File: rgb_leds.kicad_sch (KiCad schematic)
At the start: 14 parts

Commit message: Reannotate the board
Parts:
- renumbered C1401 to C55, C1402 to C56, C1403 to C57, C1404 to C58, C1405 to C59, C1406 to C60, D1401 to D15, D1402 to D16, LED1401 to LED1, LED1402 to LED2, LED1403 to LED3, LED1404 to LED4, LED1405 to LED5, TP1401 to TP26
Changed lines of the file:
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@@
 		(dnp no)
 		(fields_autoplaced yes)
-		(property "Reference" "C1403"
+		(property "Reference" "C57"
 			(at 125.73 119.3799 0)
 			(effects
@@
 			(project "HALPI2"
 				(path "/abc482bd-3f17-4d35-80db-1da3dcdb5c27/850df4bf-e40a-4082-adc2-76804638b949/7441bc5f-8874-43c2-af8a-50459ea25028"
-					(reference "C1403")
+					(reference "C57")
 					(unit 1)
 				)
@@
 		(on_board yes)
 		(dnp no)
-		(property "Reference" "#PWR01403"
+		(property "Reference" "#PWR077"
 			(at 97.79 130.81 0)
 			(effects
@@
 			(project "HALPI2"
 				(path "/abc482bd-3f17-4d35-80db-1da3dcdb5c27/850df4bf-e40a-4082-adc2-76804638b949/7441bc5f-8874-43c2-af8a-50459ea25028"
-					(reference "#PWR01403")
+					(reference "#PWR077")
 					(unit 1)
 				)
@@
 		(dnp no)
 		(fields_autoplaced yes)
-		(property "Reference" "C1405"
+		(property "Reference" "C59"
 			(at 156.21 119.3799 0)
 			(effects
@@
 			(project "HALPI2"
 				(path "/abc482bd-3f17-4d35-80db-1da3dcdb5c27/850df4bf-e40a-4082-adc2-76804638b949/7441bc5f-8874-43c2-af8a-50459ea25028"
-					(reference "C1405")
+					(reference "C59")
 					(unit 1)
 				)
@@
 		(dnp no)
 		(fields_autoplaced yes)
-		(property "Reference" "C1404"
+		(property "Reference" "C58"
 			(at 140.97 119.3799 0)
 			(effects
@@
 			(project "HALPI2"
 				(path "/abc482bd-3f17-4d35-80db-1da3dcdb5c27/850df4bf-e40a-4082-adc2-76804638b949/7441bc5f-8874-43c2-af8a-50459ea25028"
-					(reference "C1404")
+					(reference "C58")
 					(unit 1)
 				)
@@
 		(on_board yes)
 		(dnp no)
-		(property "Reference" "#PWR01407"
+		(property "Reference" "#PWR081"
 			(at 152.4 130.81 0)
 			(effects
@@
 			(project "HALPI2"
 				(path "/abc482bd-3f17-4d35-80db-1da3dcdb5c27/850df4bf-e40a-4082-adc2-76804638b949/7441bc5f-8874-43c2-af8a-50459ea25028"
-					(reference "#PWR01407")
+					(reference "#PWR081")
 					(unit 1)
 				)
@@
 		(dnp no)
 		(fields_autoplaced yes)
-		(property "Reference" "TP1401"
+		(property "Reference" "TP26"
 			(at 186.69 109.2199 90)
 			(effects
@@
 			(project "HALPI2"
 				(path "/abc482bd-3f17-4d35-80db-1da3dcdb5c27/850df4bf-e40a-4082-adc2-76804638b949/7441bc5f-8874-43c2-af8a-50459ea25028"
-					(reference "TP1401")
+					(reference "TP26")
 					(unit 1)
 				)
@@
 		(dnp no)
 		(fields_autoplaced yes)
-		(property "Reference" "#PWR01401"
+		(property "Reference" "#PWR075"
 			(at 81.28 105.41 0)
 			(effects
@@
 			(project ""
 				(path "/abc482bd-3f17-4d35-80db-1da3dcdb5c27/850df4bf-e40a-4082-adc2-76804638b949/7441bc5f-8874-43c2-af8a-50459ea25028"
-					(reference "#PWR01401")
+					(reference "#PWR075")
 					(unit 1)
 				)
@@
 		(on_board yes)
 		(dnp no)
-		(property "Reference" "#PWR01404"
+		(property "Reference" "#PWR078"
 			(at 106.68 130.81 0)
 			(effects
@@
 			(project "HALPI2"
 				(path "/abc482bd-3f17-4d35-80db-1da3dcdb5c27/850df4bf-e40a-4082-adc2-76804638b949/7441bc5f-8874-43c2-af8a-50459ea25028"
-					(reference "#PWR01404")
+					(reference "#PWR078")
 					(unit 1)
 				)
@@
 		(dnp no)
 		(fields_autoplaced yes)
-		(property "Reference" "D1402"
+		(property "Reference" "D16"
 			(at 90.17 104.4574 90)
 			(effects
@@
 			(project ""
 				(path "/abc482bd-3f17-4d35-80db-1da3dcdb5c27/850df4bf-e40a-4082-adc2-76804638b949/7441bc5f-8874-43c2-af8a-50459ea25028"
-					(reference "D1402")
+					(reference "D16")
 					(unit 1)
 				)
@@
 		(dnp no)
 		(fields_autoplaced yes)
-		(property "Reference" "#PWR01402"
+		(property "Reference" "#PWR076"
 			(at 87.63 105.41 0)
 			(effects
@@
 			(project "HALPI2"
 				(path "/abc482bd-3f17-4d35-80db-1da3dcdb5c27/850df4bf-e40a-4082-adc2-76804638b949/7441bc5f-8874-43c2-af8a-50459ea25028"
-					(reference "#PWR01402")
+					(reference "#PWR076")
 					(unit 1)
 				)
@@
 		(on_board yes)
 		(dnp no)
-		(property "Reference" "#PWR01409"
+		(property "Reference" "#PWR083"
 			(at 180.34 123.19 0)
 			(effects
@@
 			(project "HALPI2"
 				(path "/abc482bd-3f17-4d35-80db-1da3dcdb5c27/850df4bf-e40a-4082-adc2-76804638b949/7441bc5f-8874-43c2-af8a-50459ea25028"
-					(reference "#PWR01409")
+					(reference "#PWR083")
 					(unit 1)
 				)
@@
 		(on_board yes)
 		(dnp no)
-		(property "Reference" "C1401"
+		(property "Reference" "C55"
 			(at 93.98 119.3799 0)
 			(effects
@@
 			(project "HALPI2"
 				(path "/abc482bd-3f17-4d35-80db-1da3dcdb5c27/850df4bf-e40a-4082-adc2-76804638b949/7441bc5f-8874-43c2-af8a-50459ea25028"
-					(reference "C1401")
+					(reference "C55")
 					(unit 1)
 				)
@@
 		(on_board yes)
 		(dnp no)
-		(property "Reference" "#PWR01408"
+		(property "Reference" "#PWR082"
 			(at 167.64 130.81 0)
 			(effects
@@
 			(project "HALPI2"
 				(path "/abc482bd-3f17-4d35-80db-1da3dcdb5c27/850df4bf-e40a-4082-adc2-76804638b949/7441bc5f-8874-43c2-af8a-50459ea25028"
-					(reference "#PWR01408")
+					(reference "#PWR082")
 					(unit 1)
 				)
@@
 		(on_board yes)
 		(dnp no)
-		(property "Reference" "LED1402"
+		(property "Reference" "LED2"
 			(at 116.332 78.74 90)
 			(effects
@@
 			(project "HALPI2"
 				(path "/abc482bd-3f17-4d35-80db-1da3dcdb5c27/850df4bf-e40a-4082-adc2-76804638b949/7441bc5f-8874-43c2-af8a-50459ea25028"
-					(reference "LED1402")
+					(reference "LED2")
 					(unit 1)
 				)
@@
 		(on_board yes)
 		(dnp no)
-		(property "Reference" "#PWR01406"
+		(property "Reference" "#PWR080"
 			(at 137.16 130.81 0)
 			(effects
@@
 			(project "HALPI2"
 				(path "/abc482bd-3f17-4d35-80db-1da3dcdb5c27/850df4bf-e40a-4082-adc2-76804638b949/7441bc5f-8874-43c2-af8a-50459ea25028"
-					(reference "#PWR01406")
+					(reference "#PWR080")
 					(unit 1)
 				)
@@
 		(on_board yes)
 		(dnp no)
-		(property "Reference" "D1401"
+		(property "Reference" "D15"
 			(at 78.74 104.4574 90)
 			(effects
@@
 			(project "HALPI2"
 				(path "/abc482bd-3f17-4d35-80db-1da3dcdb5c27/850df4bf-e40a-4082-adc2-76804638b949/7441bc5f-8874-43c2-af8a-50459ea25028"
-					(reference "D1401")
+					(reference "D15")
 					(unit 1)
 				)
@@
 		(on_board yes)
 		(dnp no)
-		(property "Reference" "LED1404"
+		(property "Reference" "LED4"
 			(at 148.082 78.74 90)
 			(effects
@@
 			(project "HALPI2"
 				(path "/abc482bd-3f17-4d35-80db-1da3dcdb5c27/850df4bf-e40a-4082-adc2-76804638b949/7441bc5f-8874-43c2-af8a-50459ea25028"
-					(reference "LED1404")
+					(reference "LED4")
 					(unit 1)
 				)
@@
 		(dnp no)
 		(fields_autoplaced yes)
-		(property "Reference" "#FLG01401"
+		(property "Reference" "#FLG011"
 			(at 79.375 114.3 0)
 			(effects
@@
 			(project ""
 				(path "/abc482bd-3f17-4d35-80db-1da3dcdb5c27/850df4bf-e40a-4082-adc2-76804638b949/7441bc5f-8874-43c2-af8a-50459ea25028"
-					(reference "#FLG01401")
+					(reference "#FLG011")
 					(unit 1)
 				)
@@
 		(dnp no)
 		(fields_autoplaced yes)
-		(property "Reference" "C1406"
+		(property "Reference" "C60"
 			(at 171.45 119.3799 0)
 			(effects
@@
 			(project "HALPI2"
 				(path "/abc482bd-3f17-4d35-80db-1da3dcdb5c27/850df4bf-e40a-4082-adc2-76804638b949/7441bc5f-8874-43c2-af8a-50459ea25028"
-					(reference "C1406")
+					(reference "C60")
 					(unit 1)
 				)
@@
 		(dnp no)
 		(fields_autoplaced yes)
-		(property "Reference" "C1402"
+		(property "Reference" "C56"
 			(at 110.49 119.3799 0)
 			(effects
@@
 			(project "HALPI2"
 				(path "/abc482bd-3f17-4d35-80db-1da3dcdb5c27/850df4bf-e40a-4082-adc2-76804638b949/7441bc5f-8874-43c2-af8a-50459ea25028"
-					(reference "C1402")
+					(reference "C56")
 					(unit 1)
 				)
@@
 		(on_board yes)
 		(dnp no)
-		(property "Reference" "LED1403"
+		(property "Reference" "LED3"
 			(at 131.572 84.836 90)
 			(effects
@@
 			(project "HALPI2"
 				(path "/abc482bd-3f17-4d35-80db-1da3dcdb5c27/850df4bf-e40a-4082-adc2-76804638b949/7441bc5f-8874-43c2-af8a-50459ea25028"
-					(reference "LED1403")
+					(reference "LED3")
 					(unit 1)
 				)
@@
 		(on_board yes)
 		(dnp no)
-		(property "Reference" "LED1405"
+		(property "Reference" "LED5"
 			(at 166.116 85.09 90)
 			(effects
@@
 			(project "HALPI2"
 				(path "/abc482bd-3f17-4d35-80db-1da3dcdb5c27/850df4bf-e40a-4082-adc2-76804638b949/7441bc5f-8874-43c2-af8a-50459ea25028"
-					(reference "LED1405")
+					(reference "LED5")
 					(unit 1)
 				)
@@
 		(on_board yes)
 		(dnp no)
-		(property "Reference" "LED1401"
+		(property "Reference" "LED1"
 			(at 100.584 84.074 90)
 			(effects
@@
 			(project "HALPI2"
 				(path "/abc482bd-3f17-4d35-80db-1da3dcdb5c27/850df4bf-e40a-4082-adc2-76804638b949/7441bc5f-8874-43c2-af8a-50459ea25028"
-					(reference "LED1401")
+					(reference "LED1")
 					(unit 1)
 				)
@@
 		(on_board yes)
 		(dnp no)
-		(property "Reference" "#PWR01405"
+		(property "Reference" "#PWR079"
 			(at 121.92 130.81 0)
 			(effects
@@
 			(project "HALPI2"
 				(path "/abc482bd-3f17-4d35-80db-1da3dcdb5c27/850df4bf-e40a-4082-adc2-76804638b949/7441bc5f-8874-43c2-af8a-50459ea25028"
-					(reference "#PWR01405")
-					(unit 1)
-				)
+					(reference "#PWR079")
+					(unit 1)
+				)

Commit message: FInal v0.2.0 proto changes
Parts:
- renumbered C55 to C57, C56 to C58, C57 to C59, C58 to C60, C59 to C61, C60 to C62, D15 to D14, D16 to D15, TP26 to TP33
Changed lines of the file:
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@@
 		(dnp no)
 		(fields_autoplaced yes)
-		(property "Reference" "C57"
+		(property "Reference" "C59"
 			(at 125.73 119.3799 0)
 			(effects
@@
 			(project "HALPI2"
 				(path "/abc482bd-3f17-4d35-80db-1da3dcdb5c27/850df4bf-e40a-4082-adc2-76804638b949/7441bc5f-8874-43c2-af8a-50459ea25028"
-					(reference "C57")
+					(reference "C59")
 					(unit 1)
 				)
@@
 		(on_board yes)
 		(dnp no)
-		(property "Reference" "#PWR077"
+		(property "Reference" "#PWR078"
 			(at 97.79 130.81 0)
 			(effects
@@
 			(project "HALPI2"
 				(path "/abc482bd-3f17-4d35-80db-1da3dcdb5c27/850df4bf-e40a-4082-adc2-76804638b949/7441bc5f-8874-43c2-af8a-50459ea25028"
-					(reference "#PWR077")
+					(reference "#PWR078")
 					(unit 1)
 				)
@@
 		(dnp no)
 		(fields_autoplaced yes)
-		(property "Reference" "C59"
+		(property "Reference" "C61"
 			(at 156.21 119.3799 0)
 			(effects
@@
 			(project "HALPI2"
 				(path "/abc482bd-3f17-4d35-80db-1da3dcdb5c27/850df4bf-e40a-4082-adc2-76804638b949/7441bc5f-8874-43c2-af8a-50459ea25028"
-					(reference "C59")
+					(reference "C61")
 					(unit 1)
 				)
@@
 		(dnp no)
 		(fields_autoplaced yes)
-		(property "Reference" "C58"
+		(property "Reference" "C60"
 			(at 140.97 119.3799 0)
 			(effects
@@
 			(project "HALPI2"
 				(path "/abc482bd-3f17-4d35-80db-1da3dcdb5c27/850df4bf-e40a-4082-adc2-76804638b949/7441bc5f-8874-43c2-af8a-50459ea25028"
-					(reference "C58")
+					(reference "C60")
 					(unit 1)
 				)
@@
 		(on_board yes)
 		(dnp no)
-		(property "Reference" "#PWR081"
+		(property "Reference" "#PWR082"
 			(at 152.4 130.81 0)
 			(effects
@@
 			(project "HALPI2"
 				(path "/abc482bd-3f17-4d35-80db-1da3dcdb5c27/850df4bf-e40a-4082-adc2-76804638b949/7441bc5f-8874-43c2-af8a-50459ea25028"
-					(reference "#PWR081")
+					(reference "#PWR082")
 					(unit 1)
 				)
@@
 		(dnp no)
 		(fields_autoplaced yes)
-		(property "Reference" "TP26"
+		(property "Reference" "TP33"
 			(at 186.69 109.2199 90)
 			(effects
@@
 			(project "HALPI2"
 				(path "/abc482bd-3f17-4d35-80db-1da3dcdb5c27/850df4bf-e40a-4082-adc2-76804638b949/7441bc5f-8874-43c2-af8a-50459ea25028"
-					(reference "TP26")
+					(reference "TP33")
 					(unit 1)
 				)
@@
 		(dnp no)
 		(fields_autoplaced yes)
-		(property "Reference" "#PWR075"
+		(property "Reference" "#PWR076"
 			(at 81.28 105.41 0)
 			(effects
@@
 			(project ""
 				(path "/abc482bd-3f17-4d35-80db-1da3dcdb5c27/850df4bf-e40a-4082-adc2-76804638b949/7441bc5f-8874-43c2-af8a-50459ea25028"
-					(reference "#PWR075")
+					(reference "#PWR076")
 					(unit 1)
 				)
@@
 		(on_board yes)
 		(dnp no)
-		(property "Reference" "#PWR078"
+		(property "Reference" "#PWR079"
 			(at 106.68 130.81 0)
 			(effects
@@
 			(project "HALPI2"
 				(path "/abc482bd-3f17-4d35-80db-1da3dcdb5c27/850df4bf-e40a-4082-adc2-76804638b949/7441bc5f-8874-43c2-af8a-50459ea25028"
-					(reference "#PWR078")
+					(reference "#PWR079")
 					(unit 1)
 				)
@@
 		(dnp no)
 		(fields_autoplaced yes)
-		(property "Reference" "D16"
+		(property "Reference" "D15"
 			(at 90.17 104.4574 90)
 			(effects
@@
 			(project ""
 				(path "/abc482bd-3f17-4d35-80db-1da3dcdb5c27/850df4bf-e40a-4082-adc2-76804638b949/7441bc5f-8874-43c2-af8a-50459ea25028"
-					(reference "D16")
+					(reference "D15")
 					(unit 1)
 				)
@@
 		(dnp no)
 		(fields_autoplaced yes)
-		(property "Reference" "#PWR076"
+		(property "Reference" "#PWR077"
 			(at 87.63 105.41 0)
 			(effects
@@
 			(project "HALPI2"
 				(path "/abc482bd-3f17-4d35-80db-1da3dcdb5c27/850df4bf-e40a-4082-adc2-76804638b949/7441bc5f-8874-43c2-af8a-50459ea25028"
-					(reference "#PWR076")
+					(reference "#PWR077")
 					(unit 1)
 				)
@@
 		(on_board yes)
 		(dnp no)
-		(property "Reference" "#PWR083"
+		(property "Reference" "#PWR084"
 			(at 180.34 123.19 0)
 			(effects
@@
 			(project "HALPI2"
 				(path "/abc482bd-3f17-4d35-80db-1da3dcdb5c27/850df4bf-e40a-4082-adc2-76804638b949/7441bc5f-8874-43c2-af8a-50459ea25028"
-					(reference "#PWR083")
+					(reference "#PWR084")
 					(unit 1)
 				)
@@
 		(on_board yes)
 		(dnp no)
-		(property "Reference" "C55"
+		(property "Reference" "C57"
 			(at 93.98 119.3799 0)
 			(effects
@@
 			(project "HALPI2"
 				(path "/abc482bd-3f17-4d35-80db-1da3dcdb5c27/850df4bf-e40a-4082-adc2-76804638b949/7441bc5f-8874-43c2-af8a-50459ea25028"
-					(reference "C55")
+					(reference "C57")
 					(unit 1)
 				)
@@
 		(on_board yes)
 		(dnp no)
-		(property "Reference" "#PWR082"
+		(property "Reference" "#PWR083"
 			(at 167.64 130.81 0)
 			(effects
@@
 			(project "HALPI2"
 				(path "/abc482bd-3f17-4d35-80db-1da3dcdb5c27/850df4bf-e40a-4082-adc2-76804638b949/7441bc5f-8874-43c2-af8a-50459ea25028"
-					(reference "#PWR082")
+					(reference "#PWR083")
 					(unit 1)
 				)
@@
 		(on_board yes)
 		(dnp no)
-		(property "Reference" "#PWR080"
+		(property "Reference" "#PWR081"
 			(at 137.16 130.81 0)
 			(effects
@@
 			(project "HALPI2"
 				(path "/abc482bd-3f17-4d35-80db-1da3dcdb5c27/850df4bf-e40a-4082-adc2-76804638b949/7441bc5f-8874-43c2-af8a-50459ea25028"
-					(reference "#PWR080")
+					(reference "#PWR081")
 					(unit 1)
 				)
@@
 		(on_board yes)
 		(dnp no)
-		(property "Reference" "D15"
+		(property "Reference" "D14"
 			(at 78.74 104.4574 90)
 			(effects
@@
 			(project "HALPI2"
 				(path "/abc482bd-3f17-4d35-80db-1da3dcdb5c27/850df4bf-e40a-4082-adc2-76804638b949/7441bc5f-8874-43c2-af8a-50459ea25028"
-					(reference "D15")
+					(reference "D14")
 					(unit 1)
 				)
@@
 		(dnp no)
 		(fields_autoplaced yes)
-		(property "Reference" "C60"
+		(property "Reference" "C62"
 			(at 171.45 119.3799 0)
 			(effects
@@
 			(project "HALPI2"
 				(path "/abc482bd-3f17-4d35-80db-1da3dcdb5c27/850df4bf-e40a-4082-adc2-76804638b949/7441bc5f-8874-43c2-af8a-50459ea25028"
-					(reference "C60")
+					(reference "C62")
 					(unit 1)
 				)
@@
 		(dnp no)
 		(fields_autoplaced yes)
-		(property "Reference" "C56"
+		(property "Reference" "C58"
 			(at 110.49 119.3799 0)
 			(effects
@@
 			(project "HALPI2"
 				(path "/abc482bd-3f17-4d35-80db-1da3dcdb5c27/850df4bf-e40a-4082-adc2-76804638b949/7441bc5f-8874-43c2-af8a-50459ea25028"
-					(reference "C56")
+					(reference "C58")
 					(unit 1)
 				)
@@
 		(on_board yes)
 		(dnp no)
-		(property "Reference" "#PWR079"
+		(property "Reference" "#PWR080"
 			(at 121.92 130.81 0)
 			(effects
@@
 			(project "HALPI2"
 				(path "/abc482bd-3f17-4d35-80db-1da3dcdb5c27/850df4bf-e40a-4082-adc2-76804638b949/7441bc5f-8874-43c2-af8a-50459ea25028"
-					(reference "#PWR079")
-					(unit 1)
-				)
+					(reference "#PWR080")
+					(unit 1)
+				)

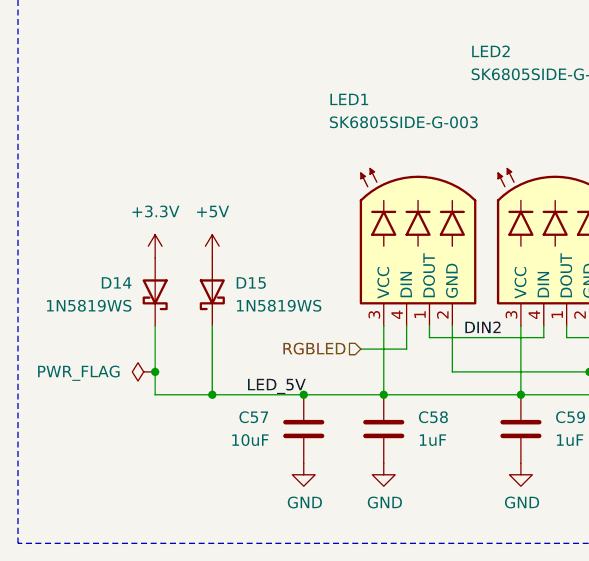
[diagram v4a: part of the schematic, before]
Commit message: Nailed the current limiter design
Also added more GND test pads
Also fixed the MCU I2C pinout
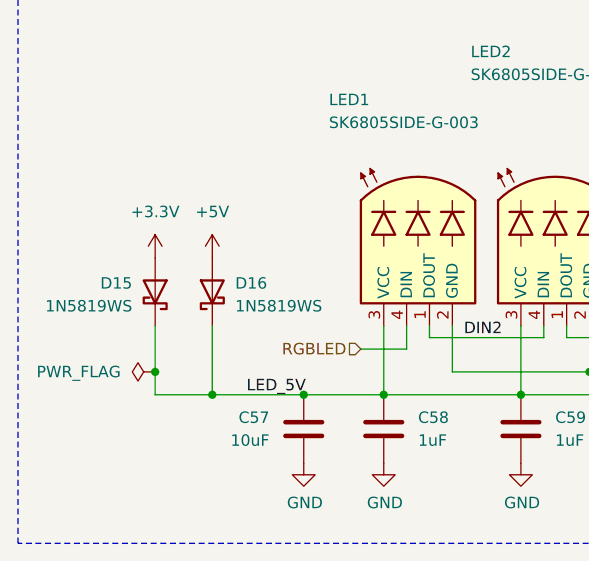
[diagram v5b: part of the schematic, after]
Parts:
- renumbered D14 to D15, D15 to D16
